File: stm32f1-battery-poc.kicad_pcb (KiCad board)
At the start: 4 copper layers, 144 parts, among them J1 Conn_01x02, J10 Conn_02x03_Odd_Even, J11 Conn_02x03_Odd_Even, J12 Conn_02x03_Odd_Even, J2 Conn_02x02_Odd_Even, J3 Conn_02x03_Odd_Even, J4 Conn_02x07_Odd_Even, J5 Conn_02x02_Odd_Even, J6 Conn_02x02_Odd_Even, J7 Conn_02x03_Odd_Even, J8 Conn_01x02, J9 Conn_01x04_Pin, M1 Stepper_Motor_bipolar, M2 Motor_3_Phases, Q1 Q_NMOS, Q2 Q_NMOS, SW1 SW_Push, SW2 SW_Push, SW3 SW_Push, SW4 SW_SPST, U1 LM78M05, U10 DRV8311H, U2 HT753-1, U3 SN65HVD230, U4 QRE1113GR, U5 QRE1113GR, U6 QRE1113GR, U7 DRV8424RGER, U8 STM32F103C8Tx, U9 BQ77905, Y1 8M

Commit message: pcb: initial rough layout
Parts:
- moved M1 168.5 mm to (264.3, 65.9), turned to 90 degrees
- moved C5 165.3 mm to (271.3, 29.2)
- moved U7 165.2 mm to (255.5, 61.6), turned to 180 degrees
- moved J2 163.5 mm to (247.5, 53.6), turned to -90 degrees
- moved J5 161.0 mm to (247.5, 63.9), turned to 180 degrees
- moved R5 160.7 mm to (271.8, 24.5)
- moved J6 159.1 mm to (242.5, 62.6), turned to 180 degrees
- moved C4 156.0 mm to (261.3, 29.2)
- moved R12 154.4 mm to (271.8, 27.0)
- moved R4 151.5 mm to (261.8, 24.5)
- moved TP8 148.0 mm to (272.0, 145.1), turned to 180 degrees
- moved C3 145.9 mm to (250.3, 29.2)
- moved TP6 145.4 mm to (268.0, 145.1), turned to 180 degrees
- moved R11 145.2 mm to (261.8, 27.0)
- moved TP3 142.7 mm to (263.0, 104.1)
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
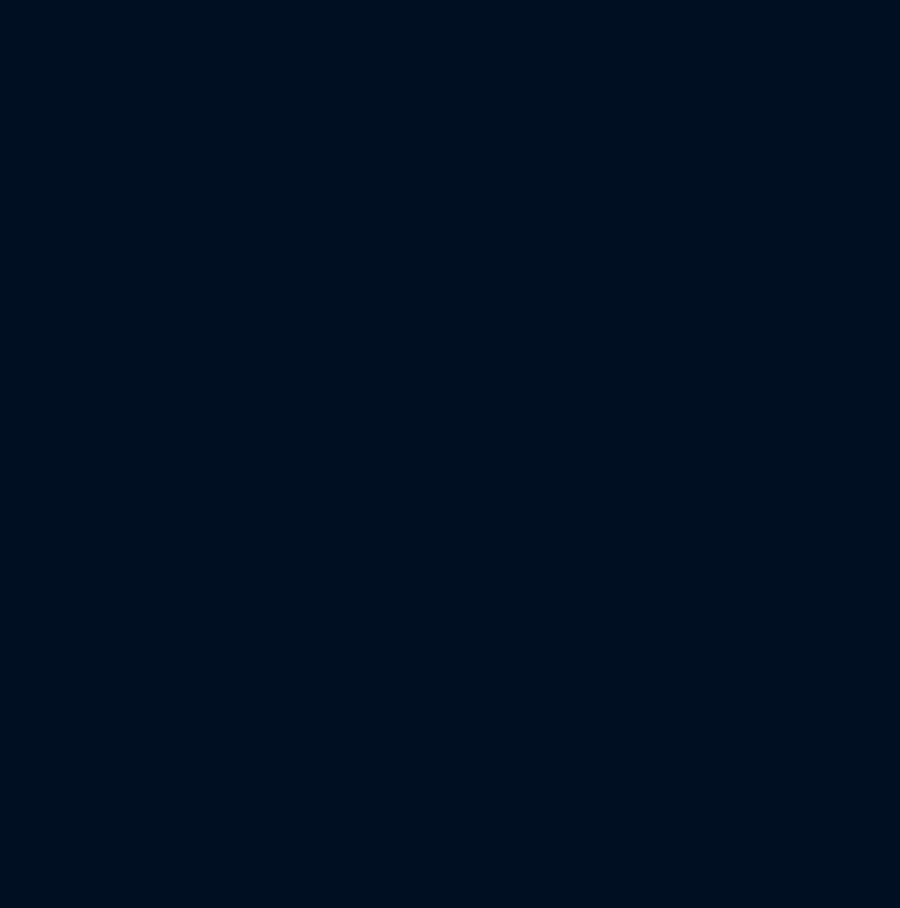
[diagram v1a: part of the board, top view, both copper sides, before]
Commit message: schem/pcb: add fiducials, mounting and tooling holes
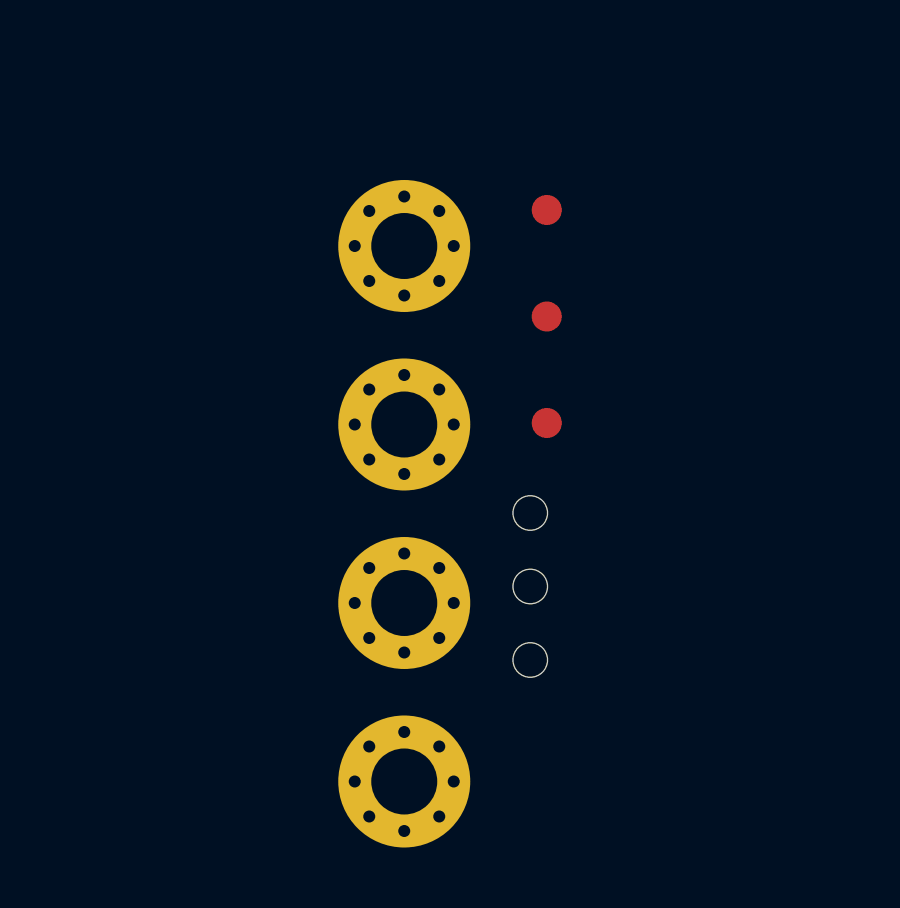
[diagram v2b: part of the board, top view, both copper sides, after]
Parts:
- added FID1: Fiducial, Fiducial:Fiducial_1mm_Mask2mm, F.Cu at (36.6, 164.8)
- added FID2: Fiducial, Fiducial:Fiducial_1mm_Mask2mm, F.Cu at (36.6, 168.3)
- added FID3: Fiducial, Fiducial:Fiducial_1mm_Mask2mm, F.Cu at (36.6, 171.9)
- added H1: MountingHole_Pad, MountingHole:MountingHole_2.2mm_M2_Pad_Via, F.Cu at (31.8, 166.0)
- added H2: MountingHole_Pad, MountingHole:MountingHole_2.2mm_M2_Pad_Via, F.Cu at (31.8, 171.9)
- added H3: MountingHole_Pad, MountingHole:MountingHole_2.2mm_M2_Pad_Via, F.Cu at (31.8, 177.9)
- added H4: MountingHole_Pad, MountingHole:MountingHole_2.2mm_M2_Pad_Via, F.Cu at (31.8, 183.8)
- added H5: MountingHole, MountingHole:ToolingHole_1.152mm, F.Cu at (36.0, 174.9)
- added H6: MountingHole, MountingHole:ToolingHole_1.152mm, F.Cu at (36.0, 177.3)
- added H7: MountingHole, MountingHole:ToolingHole_1.152mm, F.Cu at (36.0, 179.8)

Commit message: schem/pcb: change jumpers to smd
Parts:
- BT1, BT2, BT3: moved to B.Cu
- J10, J11, J12, J3, J7: footprint Connector_PinHeader_1.27mm:PinHeader_2x03_P1.27mm_Vertical -> Connector_PinHeader_1.27mm:PinHeader_2x03_P1.27mm_Vertical_SMD
- J2, J5, J6: footprint Connector_PinHeader_1.27mm:PinHeader_2x02_P1.27mm_Vertical -> Connector_PinHeader_1.27mm:PinHeader_2x02_P1.27mm_Vertical_SMD
- JP1, JP2, JP4: footprint Connector_PinHeader_1.27mm:PinHeader_2x01_P1.27mm_Vertical -> Connector_PinHeader_1.27mm:PinHeader_2x01_P1.27mm_Vertical_SMD
- JP3: footprint Connector_PinHeader_2.54mm:PinHeader_1x03_P2.54mm_Vertical -> Connector_PinHeader_1.27mm:PinHeader_1x03_P1.27mm_Vertical_SMD_Pin1Left
- moved J8 233.1 mm to (32.9, 35.3), turned to 0 degrees
- moved D5 221.5 mm to (35.9, 44.0), turned to 0 degrees
- moved TP13 155.4 mm to (69.0, 99.0), turned to 180 degrees
- moved TH1 154.3 mm to (73.0, 106.0), turned to 90 degrees
- moved R36 151.0 mm to (69.0, 94.0), turned to 90 degrees
- moved R35 149.0 mm to (72.7, 99.0), turned to 90 degrees
- moved D7 147.3 mm to (71.6, 95.0), turned to 90 degrees
- moved TP14 145.0 mm to (71.0, 91.0), turned to 180 degrees
- moved D6 144.7 mm to (74.6, 98.0), turned to -90 degrees
- moved R34 142.9 mm to (73.6, 94.2), turned to 90 degrees
- moved R31 141.9 mm to (78.0, 101.0), turned to 90 degrees
- moved D2 141.1 mm to (76.7, 167.6)
- moved JP3 141.1 mm to (80.7, 165.8)
- moved R6 141.1 mm to (76.5, 169.6)
- moved TP2 141.1 mm to (85.0, 165.6)
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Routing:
- net Net-(BT2--): track 0.00 -> 1.17 mm

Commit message: pcb: initial placement
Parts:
- removed TP12: TestPoint, TestPoint:TestPoint_Pad_D2.0mm
- moved JP2 148.8 mm to (117.6, 115.7), turned to -90 degrees
- moved M2 147.5 mm to (164.4, 50.7), turned to -90 degrees
- moved J1 146.1 mm to (123.9, 121.8), turned to -90 degrees
- moved R8 143.5 mm to (122.6, 117.7), turned to 180 degrees
- moved TP8 140.5 mm to (158.8, 61.7), turned to 0 degrees
- moved C42 138.6 mm to (172.8, 48.7), turned to 180 degrees
- moved U3 137.5 mm to (122.5, 111.3), turned to -90 degrees
- moved R2 137.5 mm to (125.6, 115.7), turned to 90 degrees
- moved JP1 135.7 mm to (127.6, 115.7), turned to 90 degrees
- moved C6 134.2 mm to (121.9, 106.8), turned to 0 degrees
- moved TP6 134.2 mm to (162.8, 61.7), turned to 0 degrees
- moved C39 132.2 mm to (171.8, 53.7), turned to 0 degrees
- moved C41 132.0 mm to (166.8, 58.7), turned to 90 degrees
- moved J4 131.4 mm to (139.6, 121.7), turned to -90 degrees
- moved TP3 130.7 mm to (132.9, 116.0), turned to -90 degrees
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
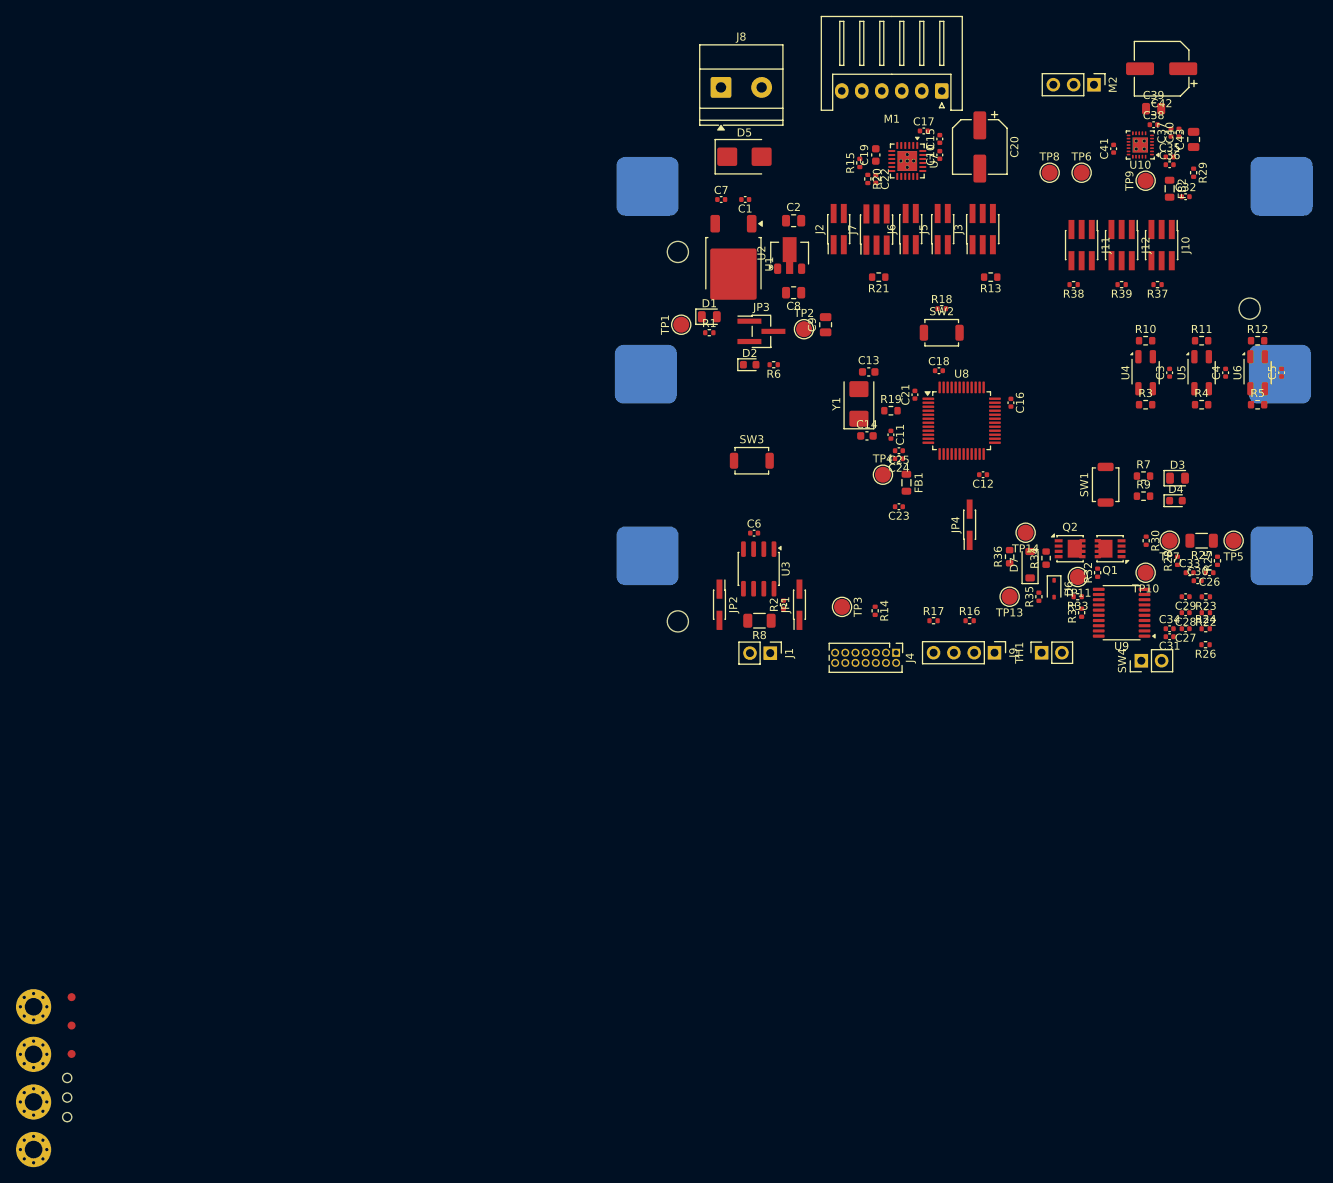
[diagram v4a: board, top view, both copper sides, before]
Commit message: pcb: add holes layout
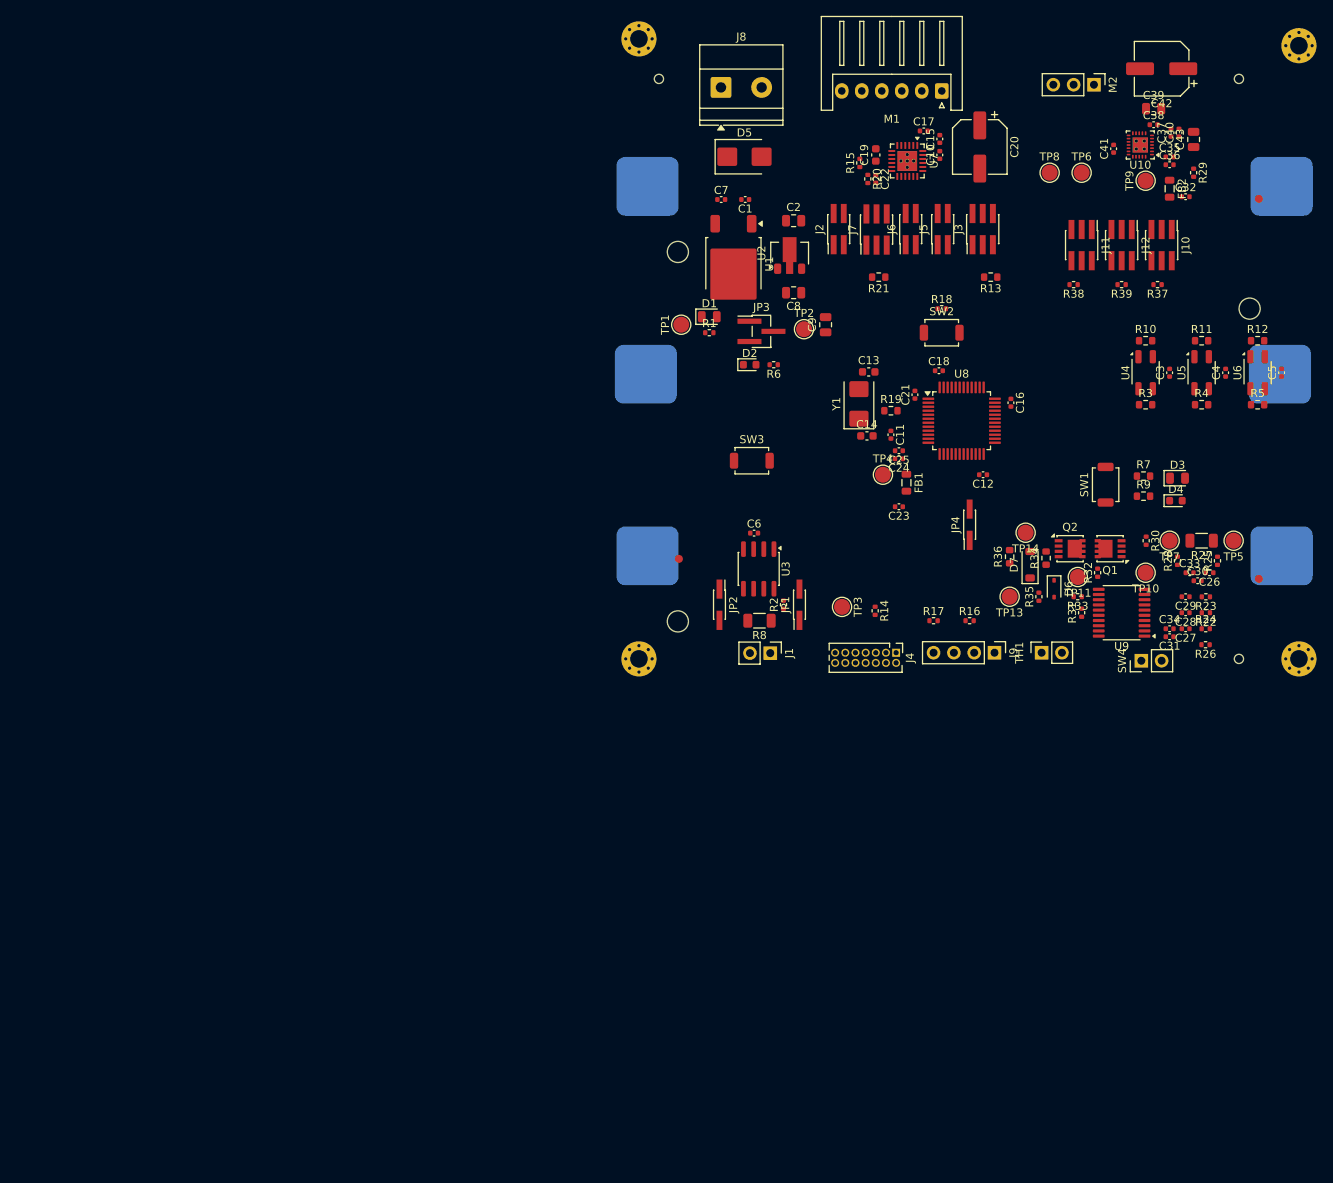
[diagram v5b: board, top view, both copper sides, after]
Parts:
- moved H3 206.0 mm to (190.0, 45.9)
- moved H7 195.7 mm to (182.5, 50.0)
- moved FID3 182.9 mm to (185.0, 65.0)
- moved H4 169.6 mm to (190.0, 122.5)
- moved FID2 158.6 mm to (185.0, 112.5)
- moved H6 156.4 mm to (182.5, 122.5)
- moved H2 147.8 mm to (107.5, 45.0)
- moved H5 145.1 mm to (110.0, 50.0)
- moved FID1 93.6 mm to (112.5, 110.0)
- moved H1 87.3 mm to (107.5, 122.5)

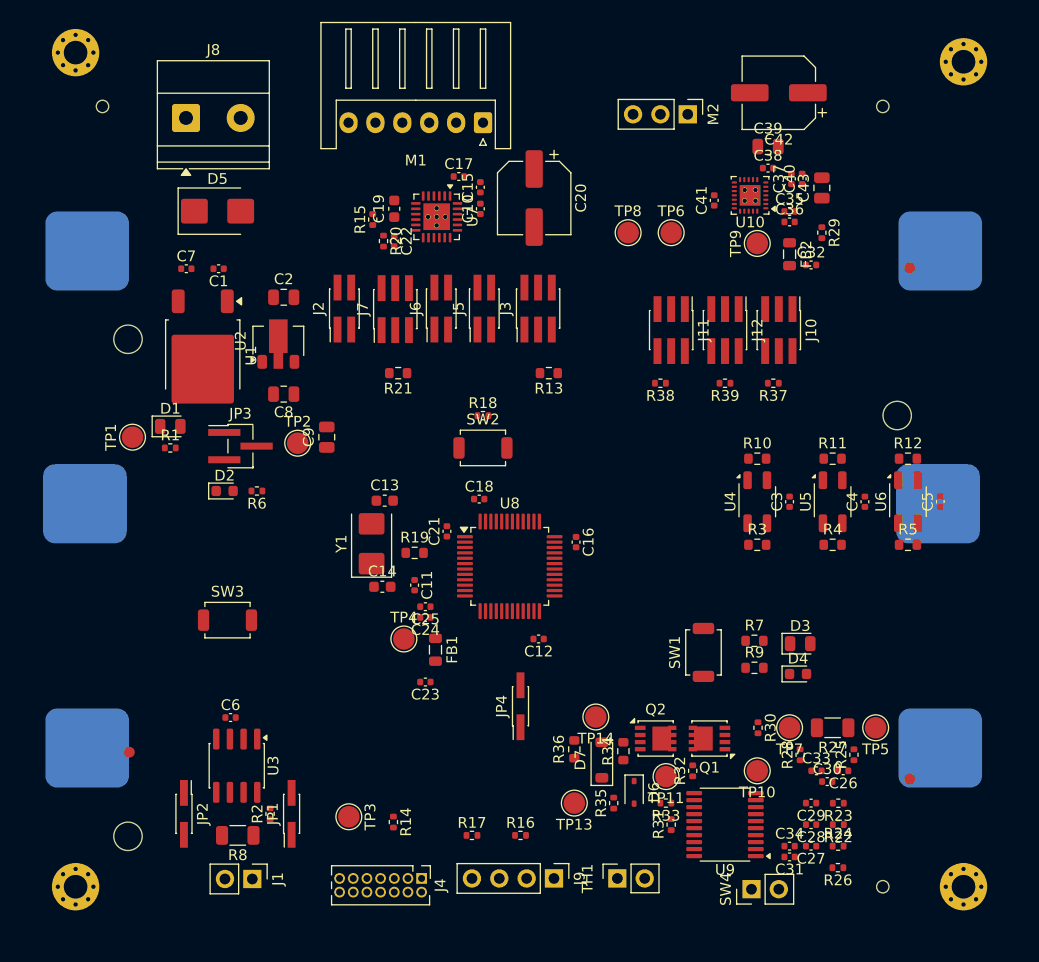
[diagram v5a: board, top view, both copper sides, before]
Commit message: pcb: add board outline
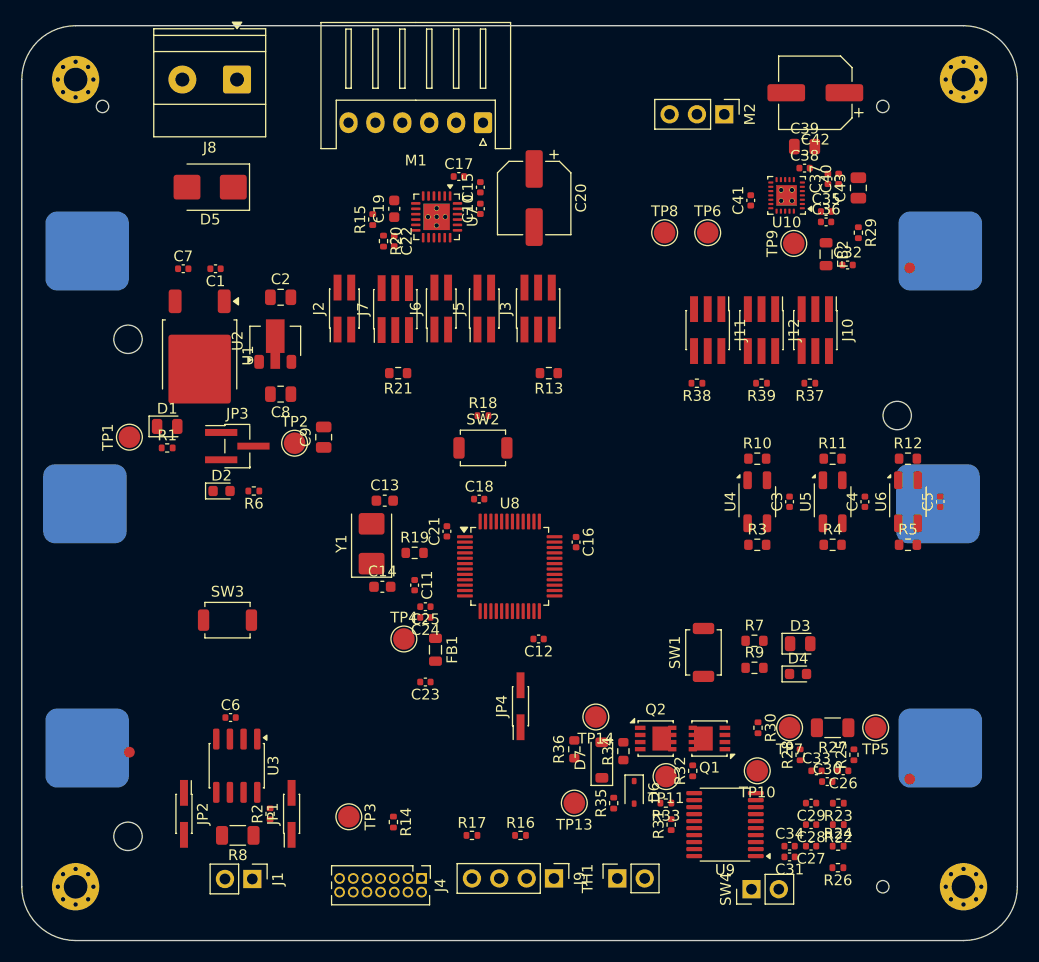
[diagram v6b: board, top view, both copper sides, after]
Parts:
- moved J8 5.94 mm to (122.5, 47.5), turned to 180 degrees
- moved C37 3.39 mm to (177.4, 56.7)
- moved C40 3.39 mm to (178.4, 56.7)
- moved M2 3.39 mm to (167.8, 50.7)
- moved R37 3.39 mm to (175.7, 75.7)
- moved U10 3.39 mm to (173.6, 58.3)
- moved C32 3.39 mm to (179.2, 64.7)
- moved C35 3.39 mm to (177.2, 59.8)
- moved C36 3.39 mm to (177.2, 60.7)
- moved C38 3.39 mm to (175.2, 55.7)
- moved C39 3.39 mm to (175.2, 53.7)
- moved C41 3.39 mm to (170.2, 58.7)
- moved C42 3.39 mm to (176.2, 48.7)
- moved C43 3.39 mm to (180.2, 57.6)
- moved FB2 3.39 mm to (177.2, 63.7)
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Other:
- board outline added: 92.5 x 85 mm
